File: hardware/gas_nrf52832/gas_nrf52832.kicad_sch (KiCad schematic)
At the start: 0 parts

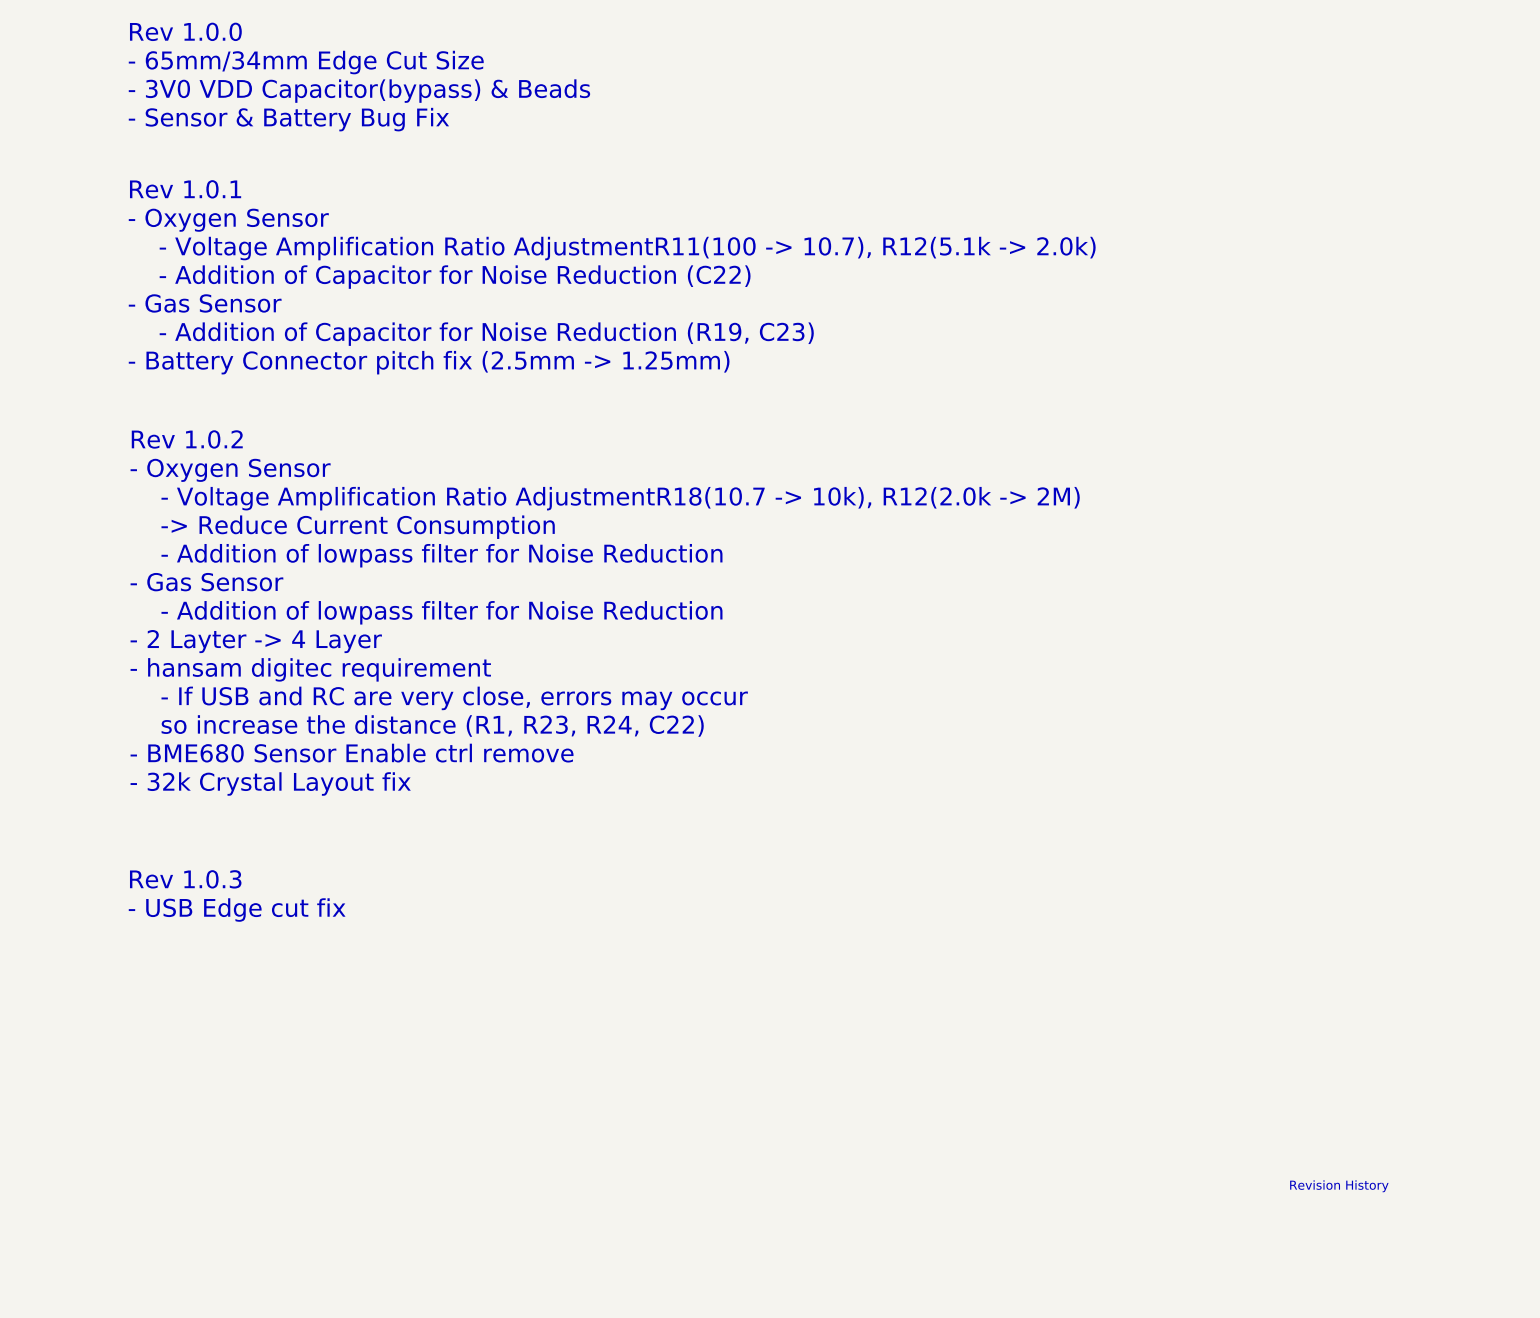
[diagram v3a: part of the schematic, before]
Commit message: test: gas biasing circuit
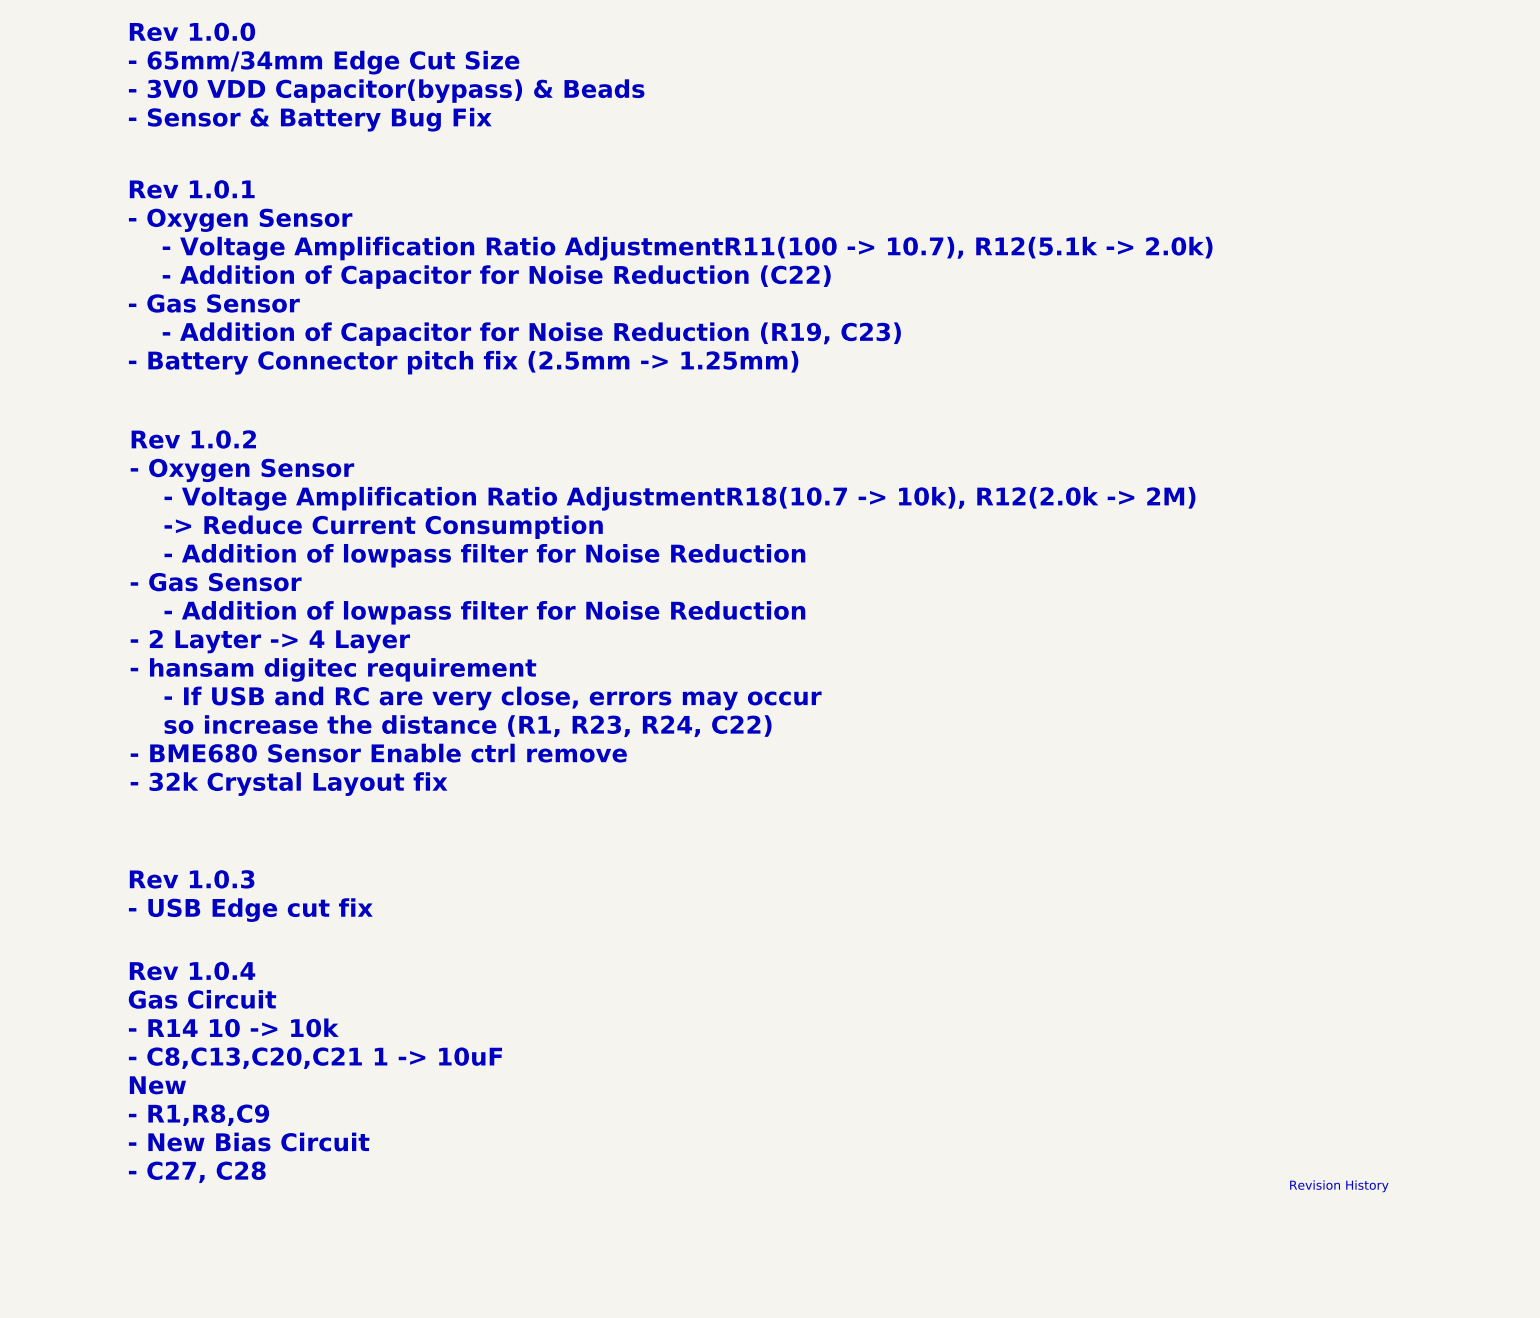
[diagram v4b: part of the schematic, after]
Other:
- note added: "Rev 1.0.4 Gas Circuit - R14 10 -> 10k - C8,C13,C20,C21 1 -> 10uF New - R1,R8,C9 - New Bias Circuit - C27, C28"
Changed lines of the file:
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@@
 			(font
 				(size 2.5 2.5)
+				(thickness 0.5)
+				(bold yes)
 			)
 			(justify left bottom)
@@
 			(font
 				(size 2.5 2.5)
+				(thickness 0.5)
+				(bold yes)
 			)
 			(justify left bottom)
@@
 			(font
 				(size 2.5 2.5)
+				(thickness 0.5)
+				(bold yes)
+			)
+			(justify left bottom)
+		)
+	)
+	(text "Rev 1.0.4\nGas Circuit\n- R14 10 -> 10k\n- C8,C13,C20,C21 1 -> 10uF\nNew\n- R1,R8,C9\n- New Bias Circuit\n- C27, C28"
+		(exclude_from_sim no)
+		(at 22.86 189.23 0)
+		(effects
+			(font
+				(size 2.5 2.5)
+				(thickness 0.5)
+				(bold yes)
 			)
 			(justify left bottom)
@@
 			(font
 				(size 2.5 2.5)
+				(thickness 0.5)
+				(bold yes)
 			)
 			(justify left bottom)

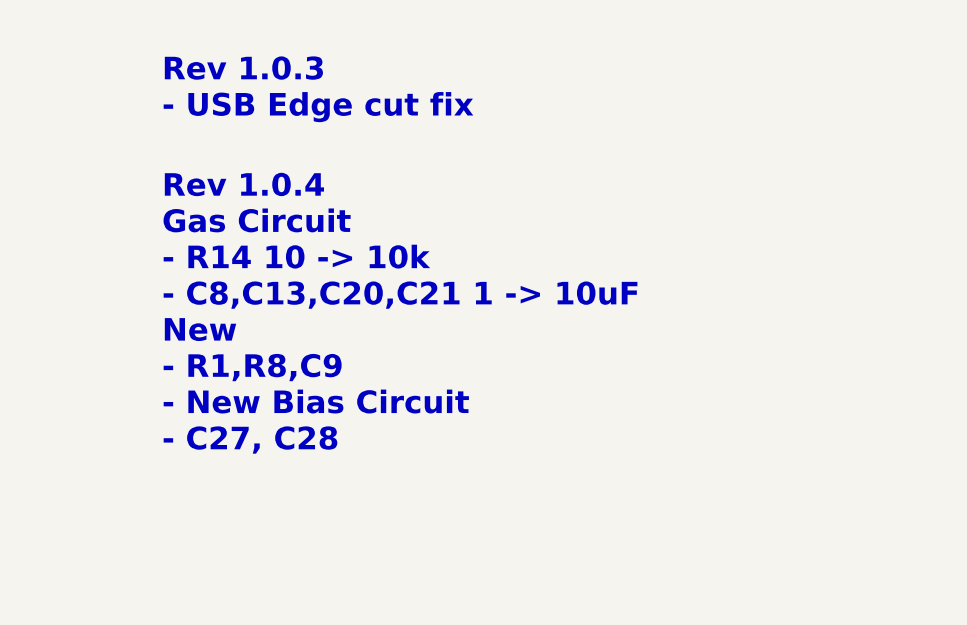
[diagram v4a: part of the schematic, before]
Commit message: feat: hw revision 1.0.4
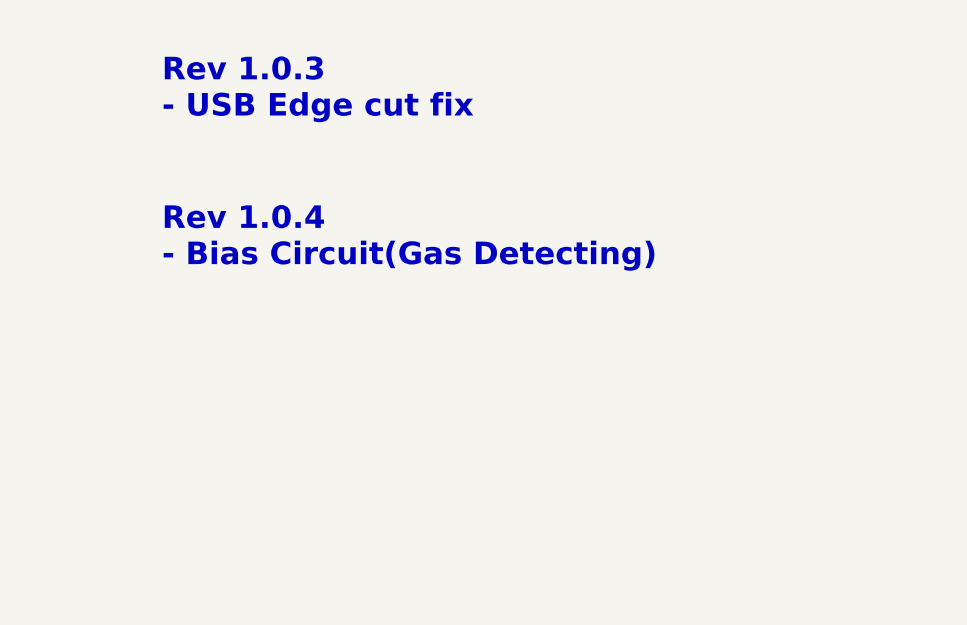
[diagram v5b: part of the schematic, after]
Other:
- note added: "Rev 1.0.4 - Bias Circuit(Gas Detecting)"
- note removed: "Rev 1.0.4 Gas Circuit - R14 10 -> 10k - C8,C13,C20,C21 1 -> 10uF New - R1,R8,C9 - New Bias Circuit - C27, C28"
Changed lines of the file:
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@@
 		)
 	)
-	(text "Rev 1.0.4\nGas Circuit\n- R14 10 -> 10k\n- C8,C13,C20,C21 1 -> 10uF\nNew\n- R1,R8,C9\n- New Bias Circuit\n- C27, C28"
+	(text "Rev 1.0.4\n- Bias Circuit(Gas Detecting)"
 		(exclude_from_sim no)
-		(at 22.86 189.23 0)
+		(at 22.86 168.656 0)
 		(effects
 			(font

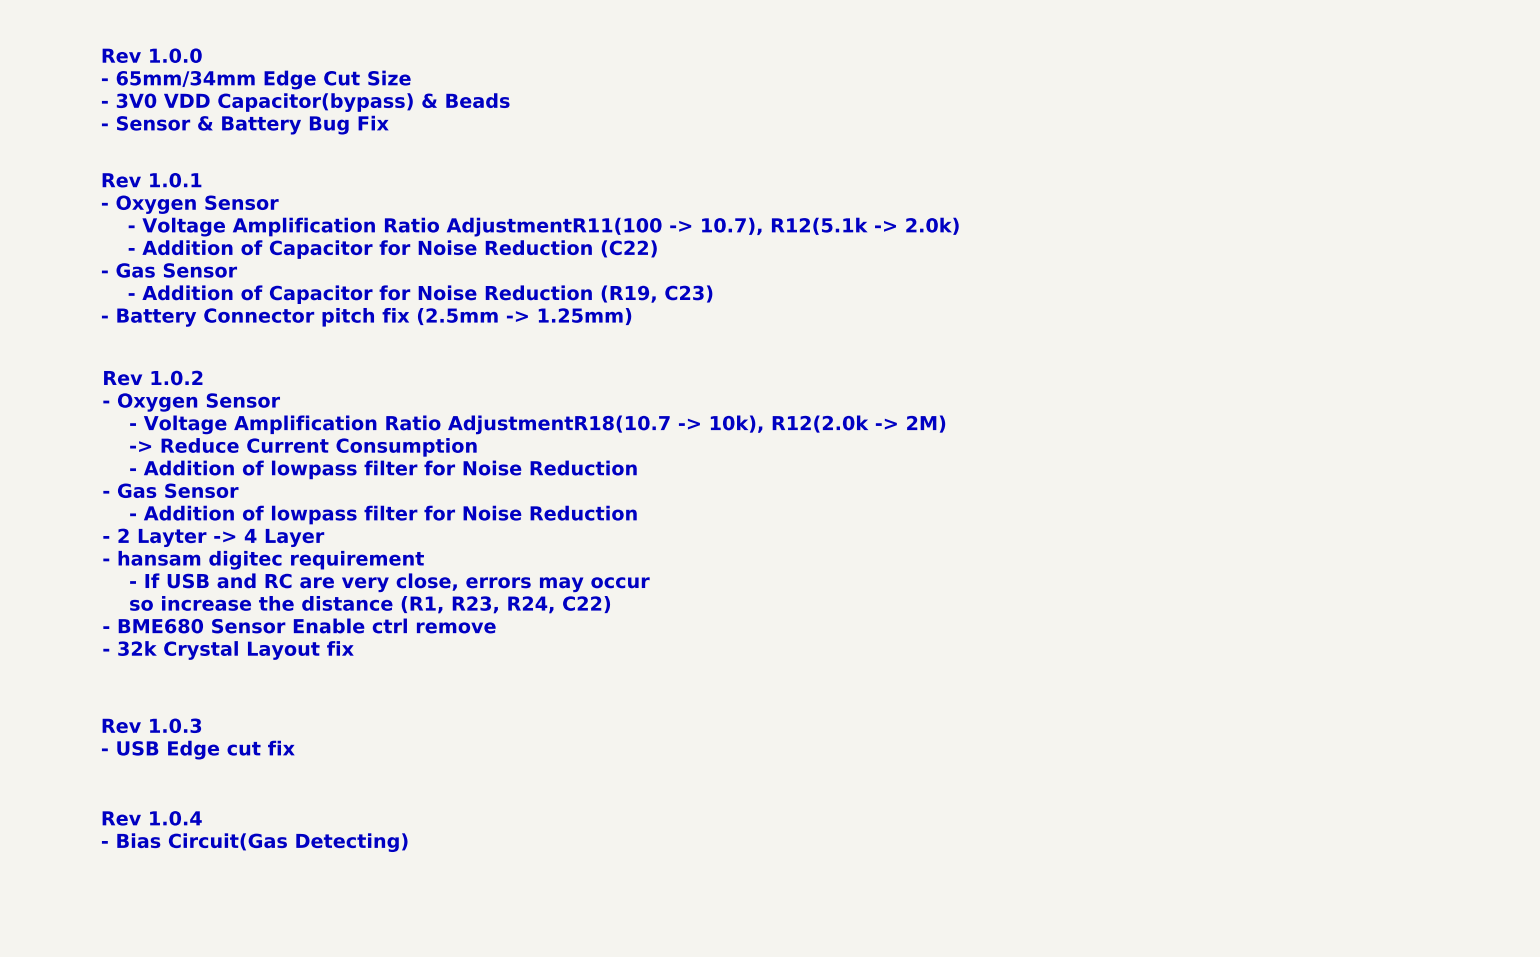
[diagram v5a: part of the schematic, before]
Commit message: feat: hw revision 2.0.1
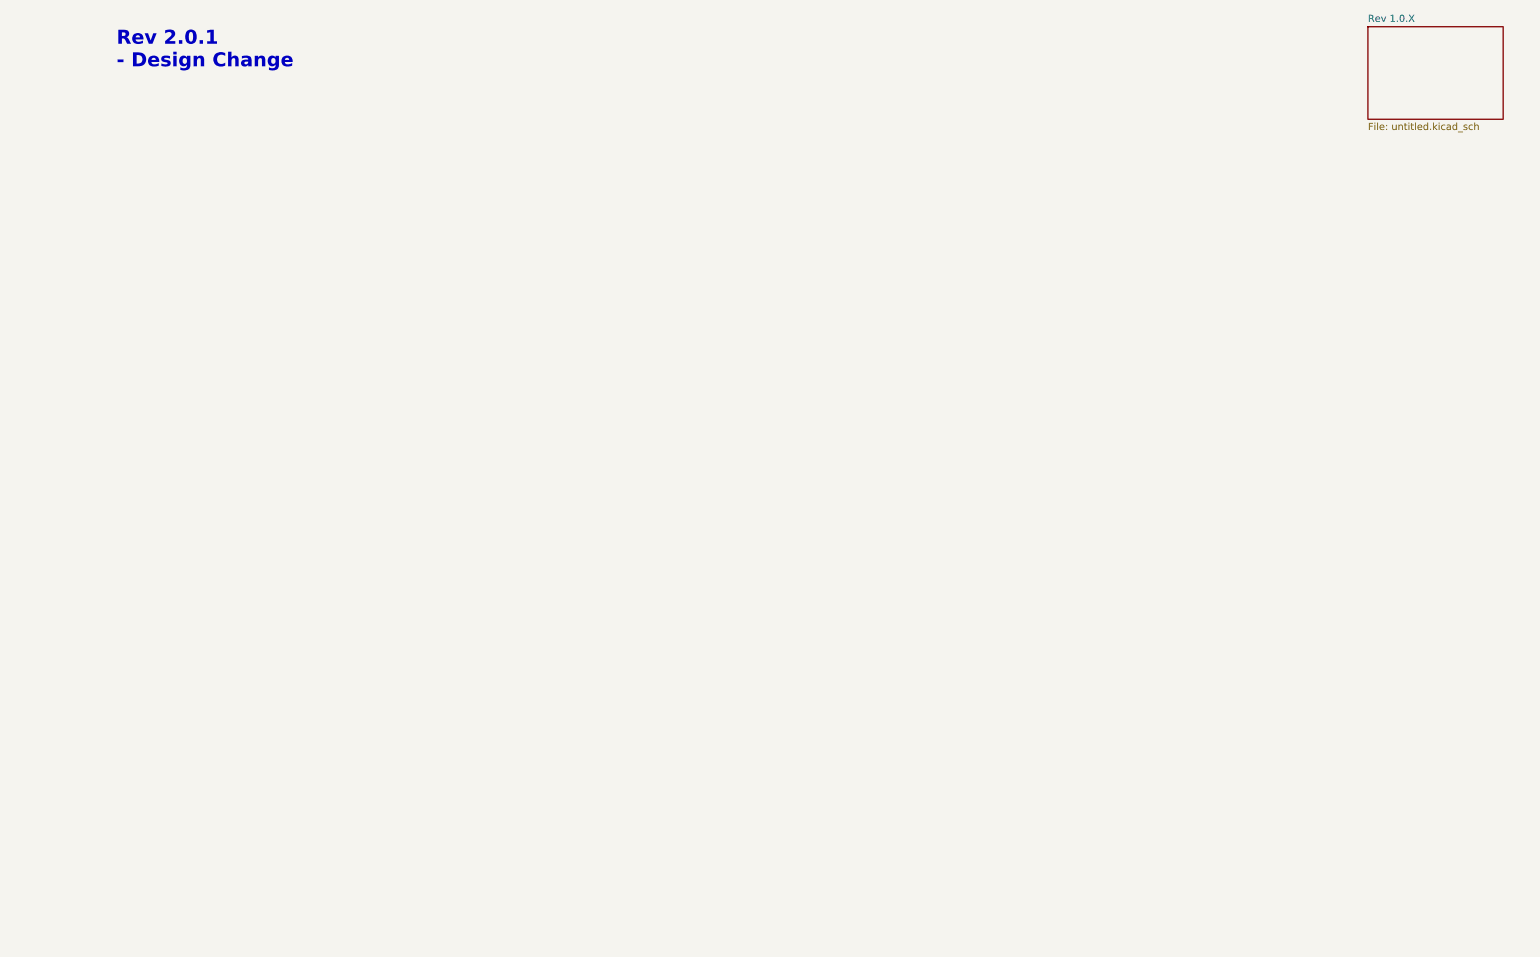
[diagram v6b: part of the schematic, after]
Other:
- added sheet Rev 1.0.X (untitled.kicad_sch)
- note added: "Rev 2.0.1 - Design Change"
- note removed: "Rev 1.0.0 - 65mm/34mm Edge Cut Size - 3V0 VDD Capacitor(bypass) & Beads - Sensor & Battery Bug Fix"
- note removed: "Rev 1.0.1 - Oxygen Sensor - Voltage Amplification Ratio AdjustmentR11(100 -> 10.7), R12(5.1k -> 2.0k) - Addition of Capacitor for Noise Reduction (C22) - Gas Sensor - Addition of Capacitor for Noise Reduction (R19, C23) - Battery Connector pitch fix (2.5mm -> 1.25mm)"
- note removed: "Rev 1.0.2 - Oxygen Sensor - Voltage Amplification Ratio AdjustmentR18(10.7 -> 10k), R12(2.0k -> 2M) -> Reduce Current Consumption - Addition of lowpass filter for Noise Reduction - Gas Sensor - Addition of lowpass filter for Noise Reduction - 2 Layter -> 4 Layer - hansam digitec requirement - If USB and RC are very close, errors may occur so increase the distance (R1, R23, R24, C22) - BME680 Sens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"
- note removed: "Rev 1.0.3 - USB Edge cut fix"
- note removed: "Rev 1.0.4 - Bias Circuit(Gas Detecting)"
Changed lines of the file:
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@@
 	(generator_version "8.0")
 	(paper "A4")
+	(title_block
+		(date "2025-01-13")
+	)
 	(text "Revision History"
 		(exclude_from_sim no)
@@
 		)
 	)
-	(text "Rev 1.0.1\n- Oxygen Sensor\n	- Voltage Amplification Ratio AdjustmentR11(100 -> 10.7), R12(5.1k -> 2.0k)\n	- Addition of Capacitor for Noise Reduction (C22)\n- Gas Sensor\n	- Addition of Capacitor for Noise Reduction (R19, C23)\n- Battery Connector pitch fix (2.5mm -> 1.25mm)"
+	(text "Rev 2.0.1\n- Design Change"
 		(exclude_from_sim no)
-		(at 22.86 74.93 0)
+		(at 25.654 29.21 0)
 		(effects
 			(font
@@
 		)
 	)
-	(text "Rev 1.0.0\n- 65mm/34mm Edge Cut Size\n- 3V0 VDD Capacitor(bypass) & Beads\n- Sensor & Battery Bug Fix"
-		(exclude_from_sim no)
-		(at 22.86 40.64 0)
-		(effects
-			(font
-				(size 2.5 2.5)
-				(thickness 0.5)
-				(bold yes)
+	(sheet
+		(at 248.92 21.59)
+		(size 24.13 16.51)
+		(fields_autoplaced yes)
+		(stroke
+			(width 0.1524)
+			(type solid)
+		)
+		(fill
+			(color 0 0 0 0.0000)
+		)
+		(property "Sheetname" "Rev 1.0.X"
+			(at 248.92 20.8784 0)
+			(effects
+				(font
+					(size 1.27 1.27)
+				)
+				(justify left bottom)
 			)
-			(justify left bottom)
+		)
+		(property "Sheetfile" "untitled.kicad_sch"
+			(at 248.92 38.6846 0)
+			(effects
+				(font
+					(size 1.27 1.27)
+				)
+				(justify left top)
+			)
+		)
+		(instances
+			(project "gas_nrf52832"
+				(path "/49921ab5-3ded-458c-bdac-830c92c2ee0e"
+					(page "5")
+				)
+			)
 		)
 	)
-	(text "Rev 1.0.2\n- Oxygen Sensor\n	- Voltage Amplification Ratio AdjustmentR18(10.7 -> 10k), R12(2.0k -> 2M)\n	-> Reduce Current Consumption\n	- Addition of lowpass filter for Noise Reduction\n- Gas Sensor\n	- Addition of lowpass filter for Noise Reduction\n- 2 Layter -> 4 Layer\n- hansam digitec requirement\n	- If USB and RC are very close, errors may occur\n	so increase the distance (R1, R23, R24, C22)\n- BME680 Sensor Enable ctrl remove\n- 32k Crystal Layout fix"
-		(exclude_from_sim no)
-		(at 23.114 134.366 0)
-		(effects
-			(font
-				(size 2.5 2.5)
-				(thickness 0.5)
-				(bold yes)
-			)
-			(justify left bottom)
-		)
-	)
-	(text "Rev 1.0.4\n- Bias Circuit(Gas Detecting)"
-		(exclude_from_sim no)
-		(at 22.86 168.656 0)
-		(effects
-			(font
-				(size 2.5 2.5)
-				(thickness 0.5)
-				(bold yes)
-			)
-			(justify left bottom)
-		)
-	)
-	(text "Rev 1.0.3\n- USB Edge cut fix"
-		(exclude_from_sim no)
-		(at 22.86 152.146 0)
-		(effects
-			(font
-				(size 2.5 2.5)
-				(thickness 0.5)
-				(bold yes)
-			)
-			(justify left bottom)
-		)
-	)
